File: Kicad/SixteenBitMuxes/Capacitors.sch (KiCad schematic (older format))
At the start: 10 parts, among them U4 CD4051B

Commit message: EEprom + PCB changes
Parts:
- C19: value C -> 42uF
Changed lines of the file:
@@
 Wire Wire Line
 	5250 5050 5350 5050
-$Comp
-L Device:C C?
-U 1 1 5E9AD5F3
-P 5500 5050
-AR Path="/5E87C69B/5E9AD5F3" Ref="C?"  Part="1"
-AR Path="/5E984186/5E9AD5F3" Ref="C?"  Part="1"
-AR Path="/5E983DF3/5E9AD5F3" Ref="C19"  Part="1"
-AR Path="/5F9F739D/5E9AD5F3" Ref="C44"  Part="1"
-F 0 "C19" V 5248 5050 50  0000 C CNN
-F 1 "C" V 5339 5050 50  0000 C CNN
-F 2 "Capacitor_SMD:C_0805_2012Metric_Pad1.15x1.40mm_HandSolder" H 5538 4900 50  0001 C CNN
-F 3 "~" H 5500 5050 50  0001 C CNN
-	1    5500 5050
-	0    1    1    0
-$EndComp
 Wire Wire Line
 	5350 4650 5300 4650
@@
 	4250 4450 4350 4450
 Connection ~ 4350 4450
+$Comp
+L Device:C C?
+U 1 1 5E9AD5F3
+P 5500 5050
+AR Path="/5E87C69B/5E9AD5F3" Ref="C?"  Part="1"
+AR Path="/5E984186/5E9AD5F3" Ref="C?"  Part="1"
+AR Path="/5E983DF3/5E9AD5F3" Ref="C19"  Part="1"
+AR Path="/5F9F739D/5E9AD5F3" Ref="C44"  Part="1"
+F 0 "C19" V 5248 5050 50  0000 C CNN
+F 1 "42uF" V 5339 5050 50  0000 C CNN
+F 2 "Capacitor_SMD:C_0805_2012Metric_Pad1.15x1.40mm_HandSolder" H 5538 4900 50  0001 C CNN
+F 3 "~" H 5500 5050 50  0001 C CNN
+	1    5500 5050
+	0    1    1    0
+$EndComp
+Wire Notes Line
+	6950 5450 2450 5450
 Wire Notes Line
 	6950 1450 6950 5450
 Wire Notes Line
-	6950 5450 2450 5450
+	2450 1450 6950 1450
 Wire Notes Line
 	2450 5450 2450 1450
-Wire Notes Line
-	2450 1450 6950 1450
 $EndSCHEMATC

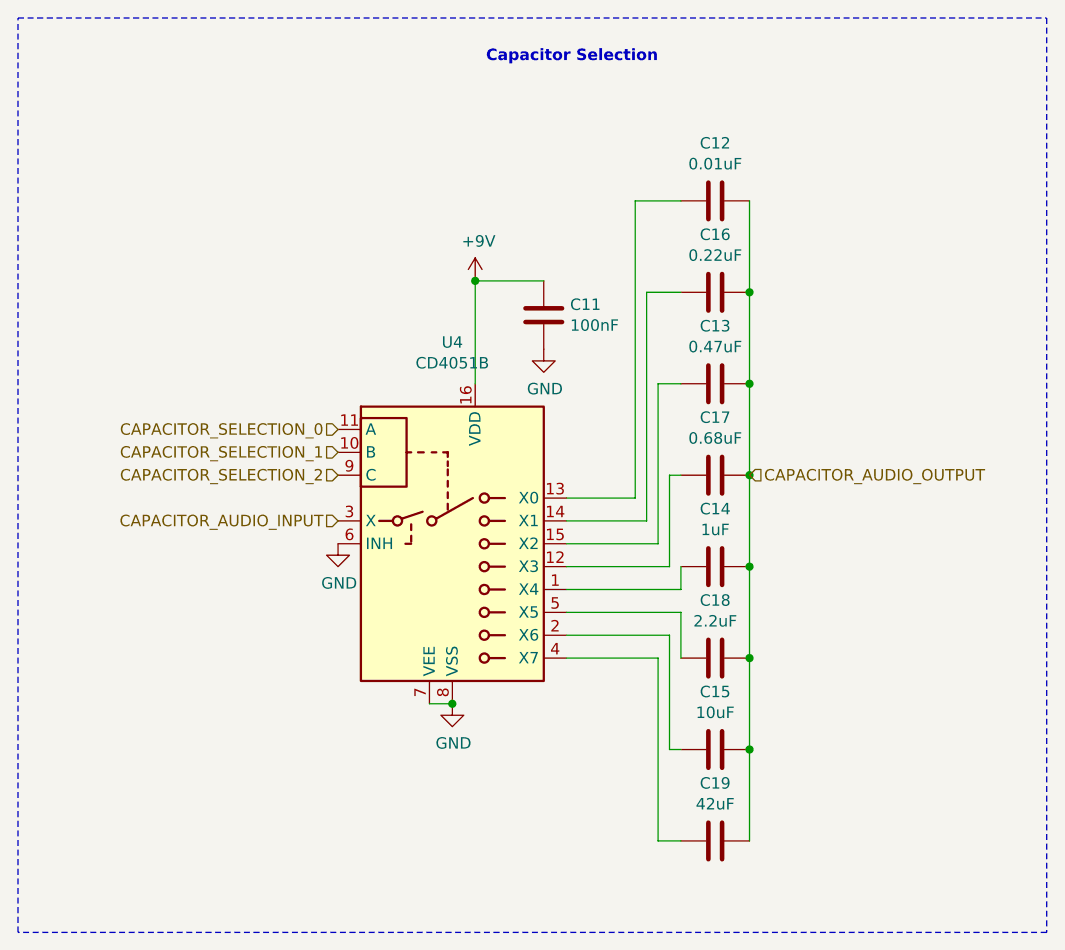
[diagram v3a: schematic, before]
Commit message: Code + resistors
Many code changes (UI) + resistors -> pulldowns.
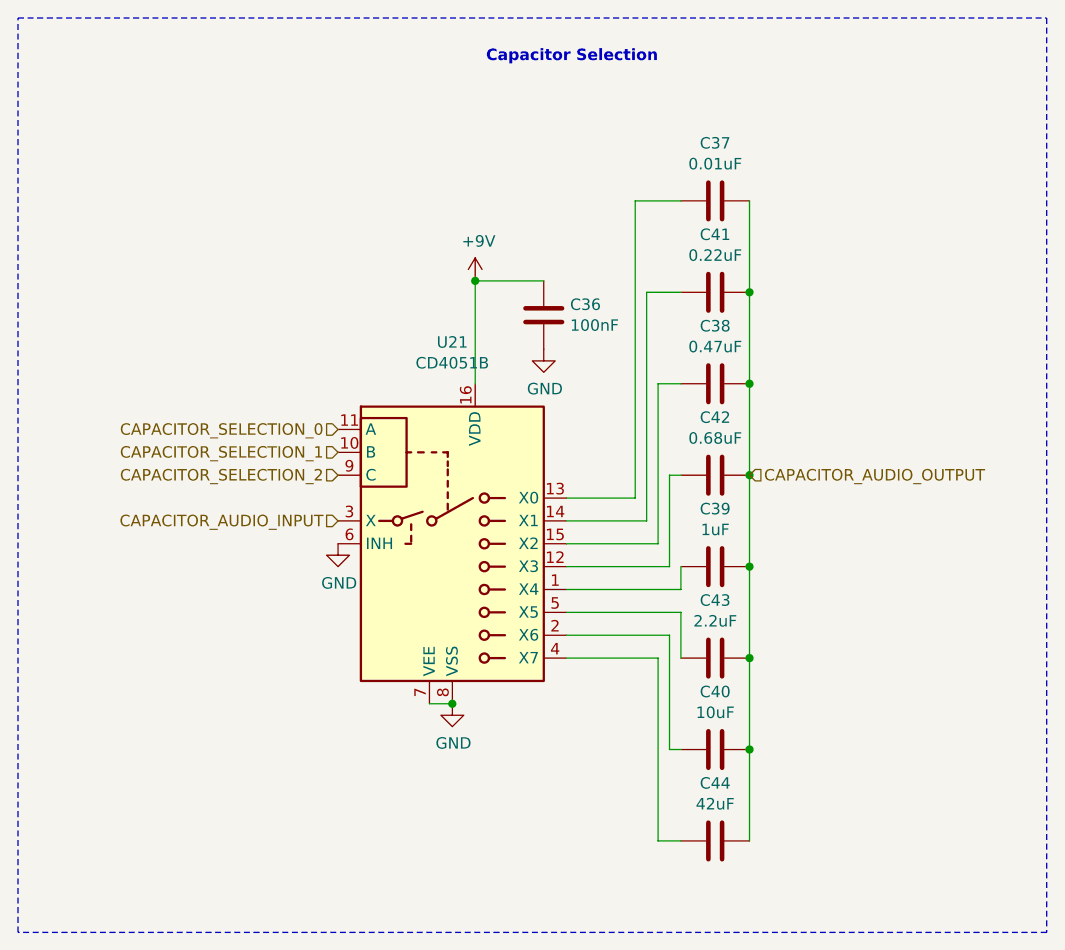
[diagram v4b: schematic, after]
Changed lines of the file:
@@
 AR Path="/5E983DF3/5E9AD572" Ref="C17"  Part="1"
 AR Path="/5F9F739D/5E9AD572" Ref="C42"  Part="1"
-F 0 "C17" V 5248 3450 50  0000 C CNN
+F 0 "C42" V 5248 3450 50  0000 C CNN
 F 1 "0.68uF" V 5339 3450 50  0000 C CNN
 F 2 "Capacitor_SMD:C_0805_2012Metric_Pad1.15x1.40mm_HandSolder" H 5538 3300 50  0001 C CNN
@@
 AR Path="/5E983DF3/5E9AD584" Ref="C16"  Part="1"
 AR Path="/5F9F739D/5E9AD584" Ref="C41"  Part="1"
-F 0 "C16" V 5248 2650 50  0000 C CNN
+F 0 "C41" V 5248 2650 50  0000 C CNN
 F 1 "0.22uF" V 5339 2650 50  0000 C CNN
 F 2 "Capacitor_SMD:C_0805_2012Metric_Pad1.15x1.40mm_HandSolder" H 5538 2500 50  0001 C CNN
@@
 AR Path="/5E983DF3/5E9AD58A" Ref="C14"  Part="1"
 AR Path="/5F9F739D/5E9AD58A" Ref="C39"  Part="1"
-F 0 "C14" V 5248 3850 50  0000 C CNN
+F 0 "C39" V 5248 3850 50  0000 C CNN
 F 1 "1uF" V 5339 3850 50  0000 C CNN
 F 2 "Capacitor_SMD:C_0805_2012Metric_Pad1.15x1.40mm_HandSolder" H 5538 3700 50  0001 C CNN
@@
 AR Path="/5E983DF3/5E9AD596" Ref="C13"  Part="1"
 AR Path="/5F9F739D/5E9AD596" Ref="C38"  Part="1"
-F 0 "C13" V 5248 3050 50  0000 C CNN
+F 0 "C38" V 5248 3050 50  0000 C CNN
 F 1 "0.47uF" V 5339 3050 50  0000 C CNN
 F 2 "Capacitor_SMD:C_0805_2012Metric_Pad1.15x1.40mm_HandSolder" H 5538 2900 50  0001 C CNN
@@
 AR Path="/5E983DF3/5E9AD59F" Ref="C11"  Part="1"
 AR Path="/5F9F739D/5E9AD59F" Ref="C36"  Part="1"
-F 0 "C11" H 4865 2796 50  0000 L CNN
+F 0 "C36" H 4865 2796 50  0000 L CNN
 F 1 "100nF" H 4865 2705 50  0000 L CNN
 F 2 "Capacitor_SMD:C_0805_2012Metric_Pad1.15x1.40mm_HandSolder" H 4788 2600 50  0001 C CNN
@@
 AR Path="/5E983DF3/5E9AD590" Ref="C12"  Part="1"
 AR Path="/5F9F739D/5E9AD590" Ref="C37"  Part="1"
-F 0 "C12" V 5248 2250 50  0000 C CNN
+F 0 "C37" V 5248 2250 50  0000 C CNN
 F 1 "0.01uF" V 5339 2250 50  0000 C CNN
 F 2 "Capacitor_SMD:C_0805_2012Metric_Pad1.15x1.40mm_HandSolder" H 5538 2100 50  0001 C CNN
@@
 AR Path="/5E983DF3/5E9AD57E" Ref="C15"  Part="1"
 AR Path="/5F9F739D/5E9AD57E" Ref="C40"  Part="1"
-F 0 "C15" V 5248 4650 50  0000 C CNN
+F 0 "C40" V 5248 4650 50  0000 C CNN
 F 1 "10uF" V 5339 4650 50  0000 C CNN
 F 2 "Capacitor_SMD:C_0805_2012Metric_Pad1.15x1.40mm_HandSolder" H 5538 4500 50  0001 C CNN
@@
 AR Path="/5E983DF3/5E9AD578" Ref="C18"  Part="1"
 AR Path="/5F9F739D/5E9AD578" Ref="C43"  Part="1"
-F 0 "C18" V 5248 4250 50  0000 C CNN
+F 0 "C43" V 5248 4250 50  0000 C CNN
 F 1 "2.2uF" V 5339 4250 50  0000 C CNN
 F 2 "Capacitor_SMD:C_0805_2012Metric_Pad1.15x1.40mm_HandSolder" H 5538 4100 50  0001 C CNN
@@
 AR Path="/5E983DF3/5E9AD56C" Ref="U4"  Part="1"
 AR Path="/5F9F739D/5E9AD56C" Ref="U21"  Part="1"
-F 0 "U4" H 4350 4631 50  0000 C CNN
+F 0 "U21" H 4350 4631 50  0000 C CNN
 F 1 "CD4051B" H 4350 4540 50  0000 C CNN
 F 2 "Package_SO:SOIC-16_3.9x9.9mm_P1.27mm" H 4500 3000 50  0001 L CNN
@@
 AR Path="/5E983DF3/5E9AD5F3" Ref="C19"  Part="1"
 AR Path="/5F9F739D/5E9AD5F3" Ref="C44"  Part="1"
-F 0 "C19" V 5248 5050 50  0000 C CNN
+F 0 "C44" V 5248 5050 50  0000 C CNN
 F 1 "42uF" V 5339 5050 50  0000 C CNN
 F 2 "Capacitor_SMD:C_0805_2012Metric_Pad1.15x1.40mm_HandSolder" H 5538 4900 50  0001 C CNN

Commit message: Improvements according video youtube
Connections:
- net +9V renamed +9V_SAFE
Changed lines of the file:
@@
 $EndComp
 Wire Wire Line
-	4450 2600 4450 3050
-Wire Wire Line
-	4750 2600 4450 2600
+	4600 3050 4450 3050
+Wire Wire Line
+	4600 2600 4600 3050
 $Comp
 L Device:C C?
@@
 	4850 4250 5250 4250
 $Comp
-L power:+9V #PWR0117
-U 1 1 5EAD3DDE
-P 4450 2600
-AR Path="/5E983DF3/5EAD3DDE" Ref="#PWR0117"  Part="1"
-AR Path="/5F9F739D/5EAD3DDE" Ref="#PWR0119"  Part="1"
-F 0 "#PWR0119" H 4450 2450 50  0001 C CNN
-F 1 "+9V" H 4465 2773 50  0000 C CNN
-F 2 "" H 4450 2600 50  0001 C CNN
-F 3 "" H 4450 2600 50  0001 C CNN
-	1    4450 2600
-	1    0    0    -1
-$EndComp
-Connection ~ 4450 2600
-$Comp
 L Analog_Switch:CD4051B U?
 U 1 1 5E9AD56C
@@
 AR Path="/5E983DF3/5E9AD56C" Ref="U4"  Part="1"
 AR Path="/5F9F739D/5E9AD56C" Ref="U21"  Part="1"
-F 0 "U21" H 4350 4631 50  0000 C CNN
-F 1 "CD4051B" H 4350 4540 50  0000 C CNN
+F 0 "U21" H 4050 4550 50  0000 C CNN
+F 1 "CD4051B" H 4050 4450 50  0000 C CNN
 F 2 "Package_SO:SOIC-16_3.9x9.9mm_P1.27mm" H 4500 3000 50  0001 L CNN
 F 3 "http://www.ti.com/lit/ds/symlink/cd4052b.pdf" H 4330 3850 50  0001 C CNN
@@
 Wire Notes Line
 	2450 5450 2450 1450
+Text HLabel 4450 3050 1    50   Input ~ 0
++9V_SAFE
+Wire Wire Line
+	4600 2600 4750 2600
 $EndSCHEMATC

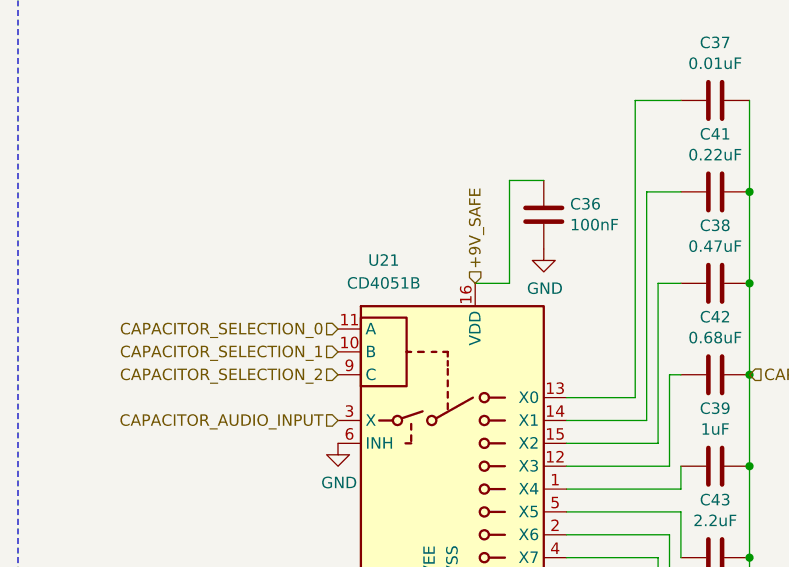
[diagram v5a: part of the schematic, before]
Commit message: UART, BOOT, NRST, Isolated OSC gnd
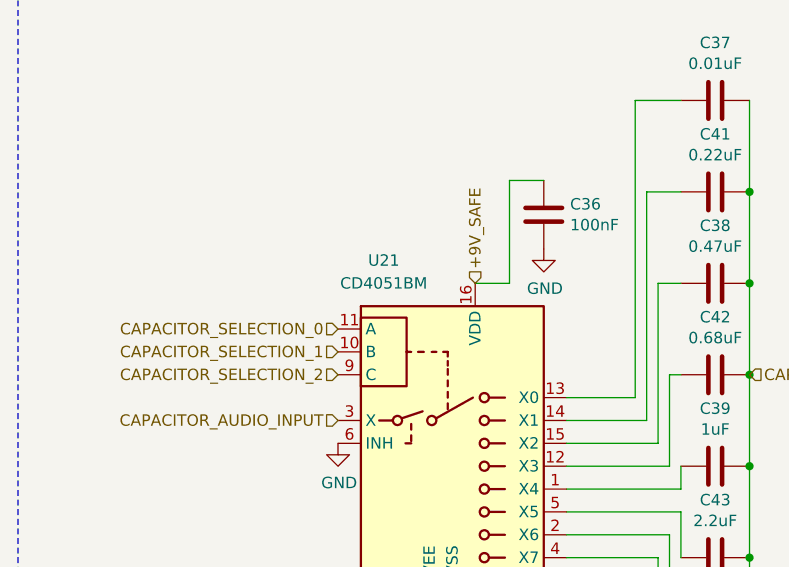
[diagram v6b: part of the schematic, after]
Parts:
- U4: value CD4051B -> CD4051BM
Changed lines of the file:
@@
 $Descr A4 11693 8268
 encoding utf-8
-Sheet 3 9
+Sheet 4 9
 Title "Guitar Pedal Effect Fuzz Digitally Controlled"
 Date "2020-04-07"
@@
 AR Path="/5F9F739D/5E9AD56C" Ref="U21"  Part="1"
 F 0 "U21" H 4050 4550 50  0000 C CNN
-F 1 "CD4051B" H 4050 4450 50  0000 C CNN
+F 1 "CD4051BM" H 4050 4450 50  0000 C CNN
 F 2 "Package_SO:SOIC-16_3.9x9.9mm_P1.27mm" H 4500 3000 50  0001 L CNN
 F 3 "http://www.ti.com/lit/ds/symlink/cd4052b.pdf" H 4330 3850 50  0001 C CNN

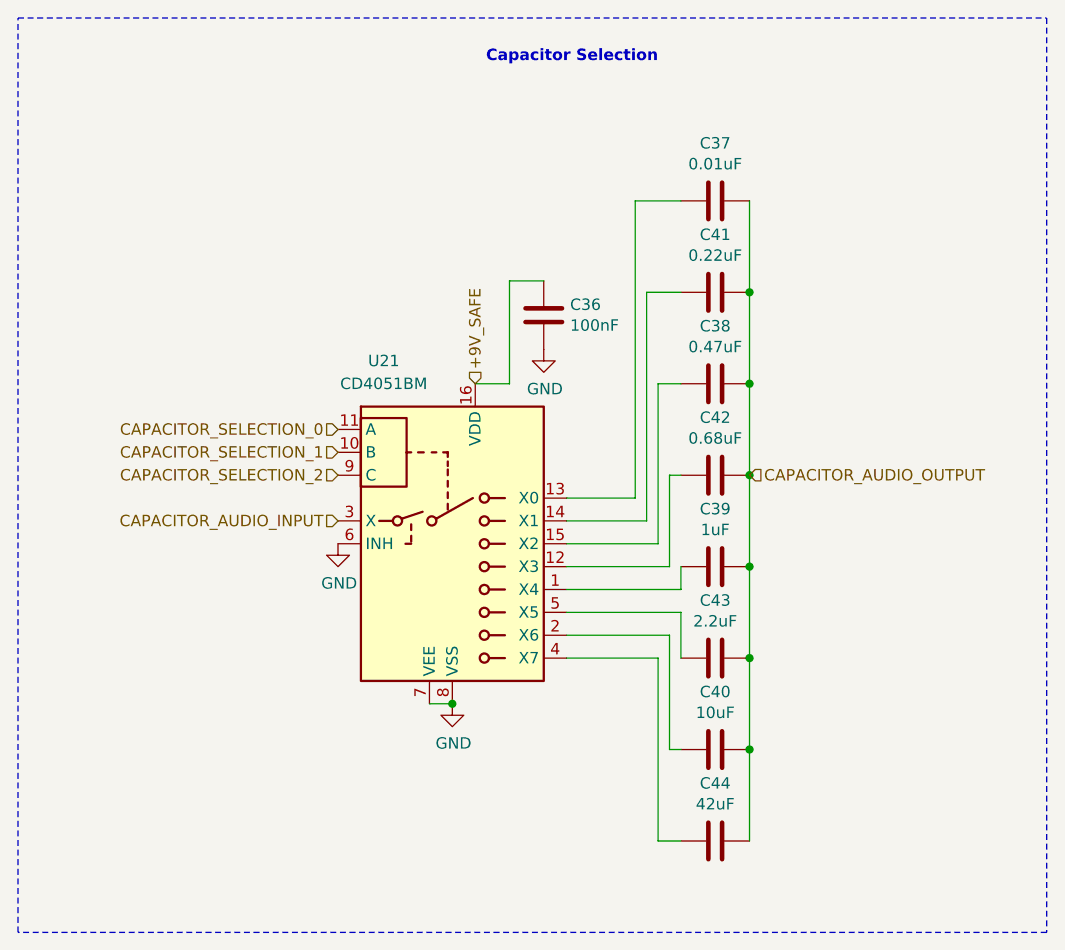
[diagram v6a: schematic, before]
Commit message: STM32 DevBoard in Freecad
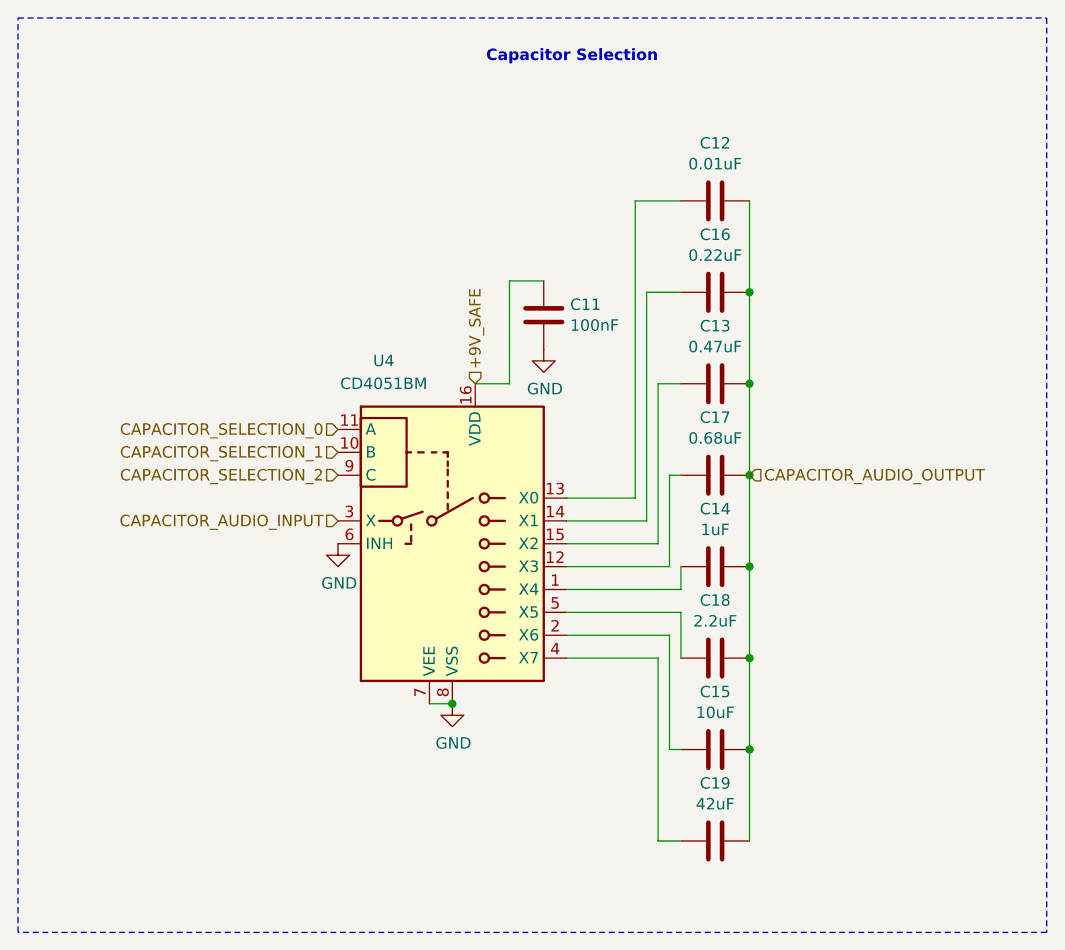
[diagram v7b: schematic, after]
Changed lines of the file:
@@
 $Descr A4 11693 8268
 encoding utf-8
-Sheet 4 9
+Sheet 3 9
 Title "Guitar Pedal Effect Fuzz Digitally Controlled"
 Date "2020-04-07"
@@
 AR Path="/5E983DF3/5E9AD572" Ref="C17"  Part="1"
 AR Path="/5F9F739D/5E9AD572" Ref="C42"  Part="1"
-F 0 "C42" V 5248 3450 50  0000 C CNN
+F 0 "C17" V 5248 3450 50  0000 C CNN
 F 1 "0.68uF" V 5339 3450 50  0000 C CNN
 F 2 "Capacitor_SMD:C_0805_2012Metric_Pad1.15x1.40mm_HandSolder" H 5538 3300 50  0001 C CNN
@@
 AR Path="/5E983DF3/5E9AD584" Ref="C16"  Part="1"
 AR Path="/5F9F739D/5E9AD584" Ref="C41"  Part="1"
-F 0 "C41" V 5248 2650 50  0000 C CNN
+F 0 "C16" V 5248 2650 50  0000 C CNN
 F 1 "0.22uF" V 5339 2650 50  0000 C CNN
 F 2 "Capacitor_SMD:C_0805_2012Metric_Pad1.15x1.40mm_HandSolder" H 5538 2500 50  0001 C CNN
@@
 AR Path="/5E983DF3/5E9AD58A" Ref="C14"  Part="1"
 AR Path="/5F9F739D/5E9AD58A" Ref="C39"  Part="1"
-F 0 "C39" V 5248 3850 50  0000 C CNN
+F 0 "C14" V 5248 3850 50  0000 C CNN
 F 1 "1uF" V 5339 3850 50  0000 C CNN
 F 2 "Capacitor_SMD:C_0805_2012Metric_Pad1.15x1.40mm_HandSolder" H 5538 3700 50  0001 C CNN
@@
 AR Path="/5E983DF3/5E9AD596" Ref="C13"  Part="1"
 AR Path="/5F9F739D/5E9AD596" Ref="C38"  Part="1"
-F 0 "C38" V 5248 3050 50  0000 C CNN
+F 0 "C13" V 5248 3050 50  0000 C CNN
 F 1 "0.47uF" V 5339 3050 50  0000 C CNN
 F 2 "Capacitor_SMD:C_0805_2012Metric_Pad1.15x1.40mm_HandSolder" H 5538 2900 50  0001 C CNN
@@
 AR Path="/5E983DF3/5E9AD59F" Ref="C11"  Part="1"
 AR Path="/5F9F739D/5E9AD59F" Ref="C36"  Part="1"
-F 0 "C36" H 4865 2796 50  0000 L CNN
+F 0 "C11" H 4865 2796 50  0000 L CNN
 F 1 "100nF" H 4865 2705 50  0000 L CNN
 F 2 "Capacitor_SMD:C_0805_2012Metric_Pad1.15x1.40mm_HandSolder" H 4788 2600 50  0001 C CNN
@@
 AR Path="/5E983DF3/5E9AD5AC" Ref="#PWR031"  Part="1"
 AR Path="/5F9F739D/5E9AD5AC" Ref="#PWR0101"  Part="1"
-F 0 "#PWR0101" H 4750 2650 50  0001 C CNN
+F 0 "#PWR031" H 4750 2650 50  0001 C CNN
 F 1 "GND" H 4755 2727 50  0000 C CNN
 F 2 "" H 4750 2900 50  0001 C CNN
@@
 AR Path="/5E983DF3/5E9AD5B2" Ref="#PWR029"  Part="1"
 AR Path="/5F9F739D/5E9AD5B2" Ref="#PWR099"  Part="1"
-F 0 "#PWR099" H 4350 4200 50  0001 C CNN
+F 0 "#PWR029" H 4350 4200 50  0001 C CNN
 F 1 "GND" H 4355 4277 50  0000 C CNN
 F 2 "" H 4350 4450 50  0001 C CNN
@@
 AR Path="/5E983DF3/5E9AD5C3" Ref="#PWR028"  Part="1"
 AR Path="/5F9F739D/5E9AD5C3" Ref="#PWR098"  Part="1"
-F 0 "#PWR098" H 3850 3500 50  0001 C CNN
+F 0 "#PWR028" H 3850 3500 50  0001 C CNN
 F 1 "GND" H 3855 3577 50  0000 C CNN
 F 2 "" H 3850 3750 50  0001 C CNN
@@
 AR Path="/5E983DF3/5E9AD590" Ref="C12"  Part="1"
 AR Path="/5F9F739D/5E9AD590" Ref="C37"  Part="1"
-F 0 "C37" V 5248 2250 50  0000 C CNN
+F 0 "C12" V 5248 2250 50  0000 C CNN
 F 1 "0.01uF" V 5339 2250 50  0000 C CNN
 F 2 "Capacitor_SMD:C_0805_2012Metric_Pad1.15x1.40mm_HandSolder" H 5538 2100 50  0001 C CNN
@@
 AR Path="/5E983DF3/5E9AD57E" Ref="C15"  Part="1"
 AR Path="/5F9F739D/5E9AD57E" Ref="C40"  Part="1"
-F 0 "C40" V 5248 4650 50  0000 C CNN
+F 0 "C15" V 5248 4650 50  0000 C CNN
 F 1 "10uF" V 5339 4650 50  0000 C CNN
 F 2 "Capacitor_SMD:C_0805_2012Metric_Pad1.15x1.40mm_HandSolder" H 5538 4500 50  0001 C CNN
@@
 AR Path="/5E983DF3/5E9AD578" Ref="C18"  Part="1"
 AR Path="/5F9F739D/5E9AD578" Ref="C43"  Part="1"
-F 0 "C43" V 5248 4250 50  0000 C CNN
+F 0 "C18" V 5248 4250 50  0000 C CNN
 F 1 "2.2uF" V 5339 4250 50  0000 C CNN
 F 2 "Capacitor_SMD:C_0805_2012Metric_Pad1.15x1.40mm_HandSolder" H 5538 4100 50  0001 C CNN
@@
 AR Path="/5E983DF3/5E9AD56C" Ref="U4"  Part="1"
 AR Path="/5F9F739D/5E9AD56C" Ref="U21"  Part="1"
-F 0 "U21" H 4050 4550 50  0000 C CNN
+F 0 "U4" H 4050 4550 50  0000 C CNN
 F 1 "CD4051BM" H 4050 4450 50  0000 C CNN
 F 2 "Package_SO:SOIC-16_3.9x9.9mm_P1.27mm" H 4500 3000 50  0001 L CNN
@@
 AR Path="/5E983DF3/5E9AD5F3" Ref="C19"  Part="1"
 AR Path="/5F9F739D/5E9AD5F3" Ref="C44"  Part="1"
-F 0 "C44" V 5248 5050 50  0000 C CNN
+F 0 "C19" V 5248 5050 50  0000 C CNN
 F 1 "42uF" V 5339 5050 50  0000 C CNN
 F 2 "Capacitor_SMD:C_0805_2012Metric_Pad1.15x1.40mm_HandSolder" H 5538 4900 50  0001 C CNN
